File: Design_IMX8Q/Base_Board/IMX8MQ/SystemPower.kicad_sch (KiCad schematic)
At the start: 71 parts, among them Q1 AO3401A, U4 MP8759GD-Z, U5 MP2263GD-Z

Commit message: Add QSPI and more color
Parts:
- removed C1, C10, C2, C3, C4, C5, C6, C7, C8, C9: 4.7uF, Capacitor_SMD:C_0402_1005Metric, symbol Device:C_Small
- removed C11, C12, C13: 22uF, Capacitor_SMD:C_0805_2012Metric, symbol Device:C_Small
- removed C14: 22uF, Capacitor_SMD:C_0402_1005Metric, symbol Device:C_Small
- removed C15, C16: 10uF, Capacitor_SMD:C_0805_2012Metric, symbol Device:C_Small
- removed C17, C64, C65, C66: 0.1uF, Capacitor_SMD:C_0402_1005Metric, symbol Device:C_Small
- removed C18, C63: 1uF, Capacitor_SMD:C_0402_1005Metric, symbol Device:C_Small
- removed C31, C32, C33, C34, C35, C36, C37, C38, C39, C40, C41, C42, C43, C44, C45, C46, C47, C55, C56, C57, C58: 22uF, Capacitor_SMD:C_0603_1608Metric, symbol Device:C_Small
- removed C48, C49, C50, C51, C52, C53: 4.7uF, Capacitor_SMD:C_0603_1608Metric, symbol Device:C_Small
- removed C54: 1uF, Capacitor_SMD:C_0603_1608Metric, symbol Device:C_Small
- removed C59: 220uF, symbol Device:C_Polarized_Small
- removed C60, C61, C62: 0.47uF, Capacitor_SMD:C_0402_1005Metric, symbol Device:C_Small
- removed L1: 1.5uH, Inductor_SMD:L_7.3x7.3_H4.5, symbol Device:L_Small
- removed L2: 4.7uH, Inductor_SMD:L_Taiyo-Yuden_NR-40xx, symbol Device:L_Small
- removed L3, L4, L5, L6, L7: 1uH, Inductor_SMD:L_Taiyo-Yuden_NR-30xx_HandSoldering, symbol Device:L_Small
- removed Q1: AO3401A, Package_TO_SOT_SMD:SOT-23, symbol Transistor_FET:AO3401A
- removed R3: 1.5M, Resistor_SMD:R_0402_1005Metric, symbol Device:R_Small
- removed R4: 44.2K, Resistor_SMD:R_0402_1005Metric, symbol Device:R_Small
- removed R5: 9.53k, Resistor_SMD:R_0402_1005Metric, symbol Device:R_Small
- removed R6, R7: 100k, Resistor_SMD:R_0402_1005Metric, symbol Device:R_Small
- removed R8: 10K, Resistor_SMD:R_0402_1005Metric, symbol Device:R_Small
- removed U3: ~, Package_DFN_QFN:QFN-56-1EP_8x8mm_P0.5mm_EP4.3x4.3mm, symbol _W_MX8M:MC34PF4210
- removed U4: MP8759GD-Z, _W_SBC:MP8759GD-Z, symbol MP8759GD-Z:MP8759GD-Z
- removed U5: MP2263GD-Z, _W_SBC:MP2263, symbol MP2263:MP2263GD-Z
- added U1: MIMX8MQ6CVAHZAB, IMX8MQ_footprints:MIMX8MQ6CVAHZAB, symbol _MIMX8MQ6CVAHZAB:MIMX8MQ6CVAHZAB
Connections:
- net GND: now also U1.A2 (VSS), U1.A24 (VSS), U1.AA16 (VSS), U1.AA21 (VSS), U1.AA5 (VSS), U1.AB11 (VSS), U1.AB18 (VSS), U1.AB2 (VSS), U1.AB24 (VSS), U1.AB9 (VSS), U1.AC19 (VSS), U1.AC22 (VSS), U1.AC4 (VSS), U1.AD1 (VSS), U1.AD11 (VSS), U1.AD13 (VSS), U1.AD16 (VSS), U1.AD25 (VSS), U1.AD7 (VSS), U1.AD9 (VSS), U1.AE2 (VSS), U1.AE21 (VSS), U1.AE24 (VSS), U1.AE5 (VSS), U1.B1 (VSS), U1.B25 (VSS), U1.C10 (VSS), U1.C13 (VSS), U1.C15 (VSS), U1.C24 (VSS), U1.C8 (VSS), U1.D10 (VSS), U1.D13 (VSS), U1.D15 (VSS), U1.D23 (VSS), U1.E10 (VSS), U1.E13 (VSS), U1.E14 (VSS), U1.E16 (VSS), U1.E19 (VSS), U1.E20 (VSS), U1.E21 (VSS), U1.E22 (VSS), U1.E23 (VSS), U1.E4 (VSS), U1.F10 (VSS), U1.F13 (VSS), U1.F14 (VSS), U1.F16 (VSS), U1.F20 (VSS), U1.G10 (VSS), U1.G13 (VSS), U1.G17 (VSS), U1.G18 (VSS), U1.G24 (VSS), U1.G9 (VSS), U1.H10 (VSS), U1.H11 (VSS), U1.H12 (VSS), U1.H13 (VSS), U1.H17 (VSS), U1.H18 (VSS), U1.H8 (VSS), U1.H9 (VSS), U1.J11 (VSS), U1.J12 (VSS), U1.J13 (VSS), U1.J14 (VSS), U1.J17 (VSS), U1.J18 (VSS), U1.J19 (VSS), U1.J3 (VSS), U1.J8 (VSS), U1.K11 (VSS), U1.K13 (VSSA_FPLL_ARM), U1.K17 (VSS), U1.K18 (VSS), U1.K23 (VSS), U1.K8 (VSS), U1.L11 (VSS), U1.L14 (VSS), U1.L17 (VSS), U1.L8 (VSS), U1.M11 (VSS), U1.M14 (VSS), U1.M17 (VSS), U1.M8 (VSS), U1.N12 (VSSA_SPLL_VIDEO2), U1.N14 (VSS), U1.N15 (VSS), U1.N16 (VSS), U1.N17 (VSS), U1.N18 (VSS), U1.N3 (VSS), U1.P11 (VSS), U1.P14 (VSS), U1.P17 (VSS), U1.P18 (VSS), U1.P23 (VSS), U1.P6 (VSS), U1.P8 (VSS), U1.R7 (VSS), U1.T10 (VSS), U1.T11 (VSS), U1.T12 (VSS), U1.T13 (VSS), U1.T14 (VSSA_SPLL_DRAM), U1.T3 (VSS), U1.T4 (VSS), U1.T9 (VSS), U1.U15 (VSS), U1.U16 (VSSA_FPLL), U1.U18 (VSS), U1.U8 (VSS), U1.U9 (VSS), U1.V16 (VSS), U1.V17 (VSSA_SPLL), U1.V23 (VSSA_XTAL_25M), U1.V4 (VSS), U1.V8 (VSS), U1.W1 (VSS), U1.W10 (VSS), U1.W11 (VSS), U1.W12 (VSS), U1.W13 (VSS), U1.W14 (VSS), U1.W15 (VSS), U1.W16 (VSS), U1.W22 (VSSA_XTAL_27M), U1.W25 (VSS), U1.W7 (VSS), U1.W8 (VSS), U1.W9 (VSS), U1.Y11 (VSS), U1.Y13 (VSS), U1.Y15 (VSS), U1.Y17 (VSS), U1.Y19 (VSS), U1.Y2 (VSS), U1.Y21 (VSS), U1.Y22 (VSS), U1.Y23 (VSS), U1.Y24 (VSS), U1.Y3 (VSS), U1.Y4 (VSS), U1.Y5 (VSS), U1.Y7 (VSS), U1.Y9 (VSS)
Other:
- note removed: "10v"
- note removed: "25v"
- note removed: "35v"
- note removed: "50v"

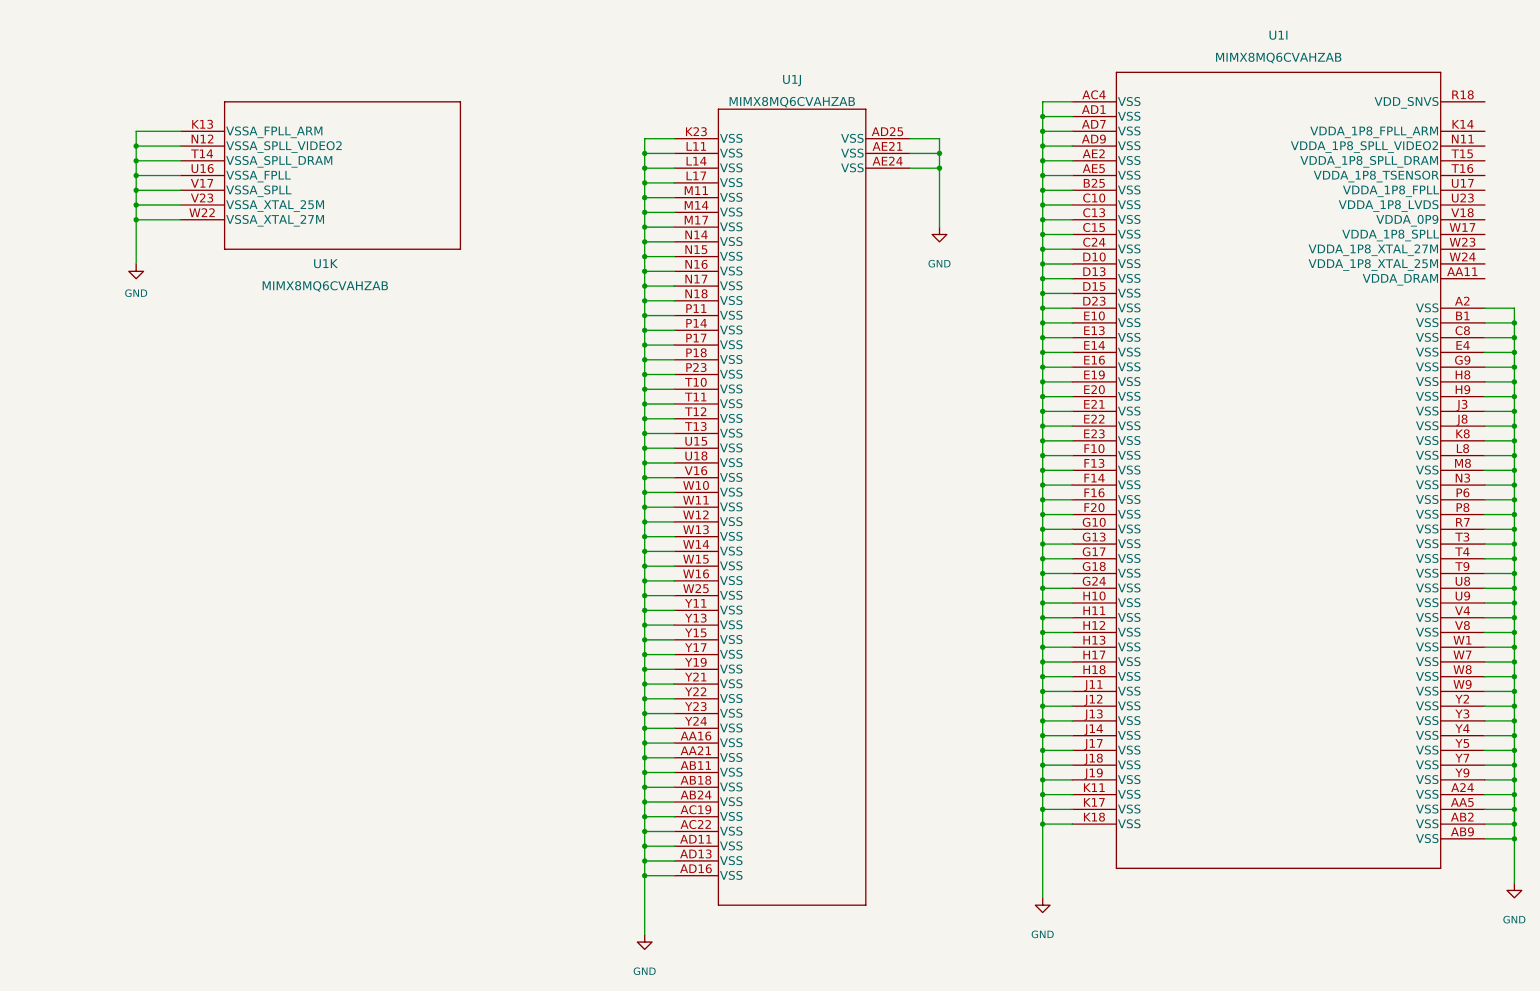
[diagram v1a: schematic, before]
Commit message: it was inserted power control system
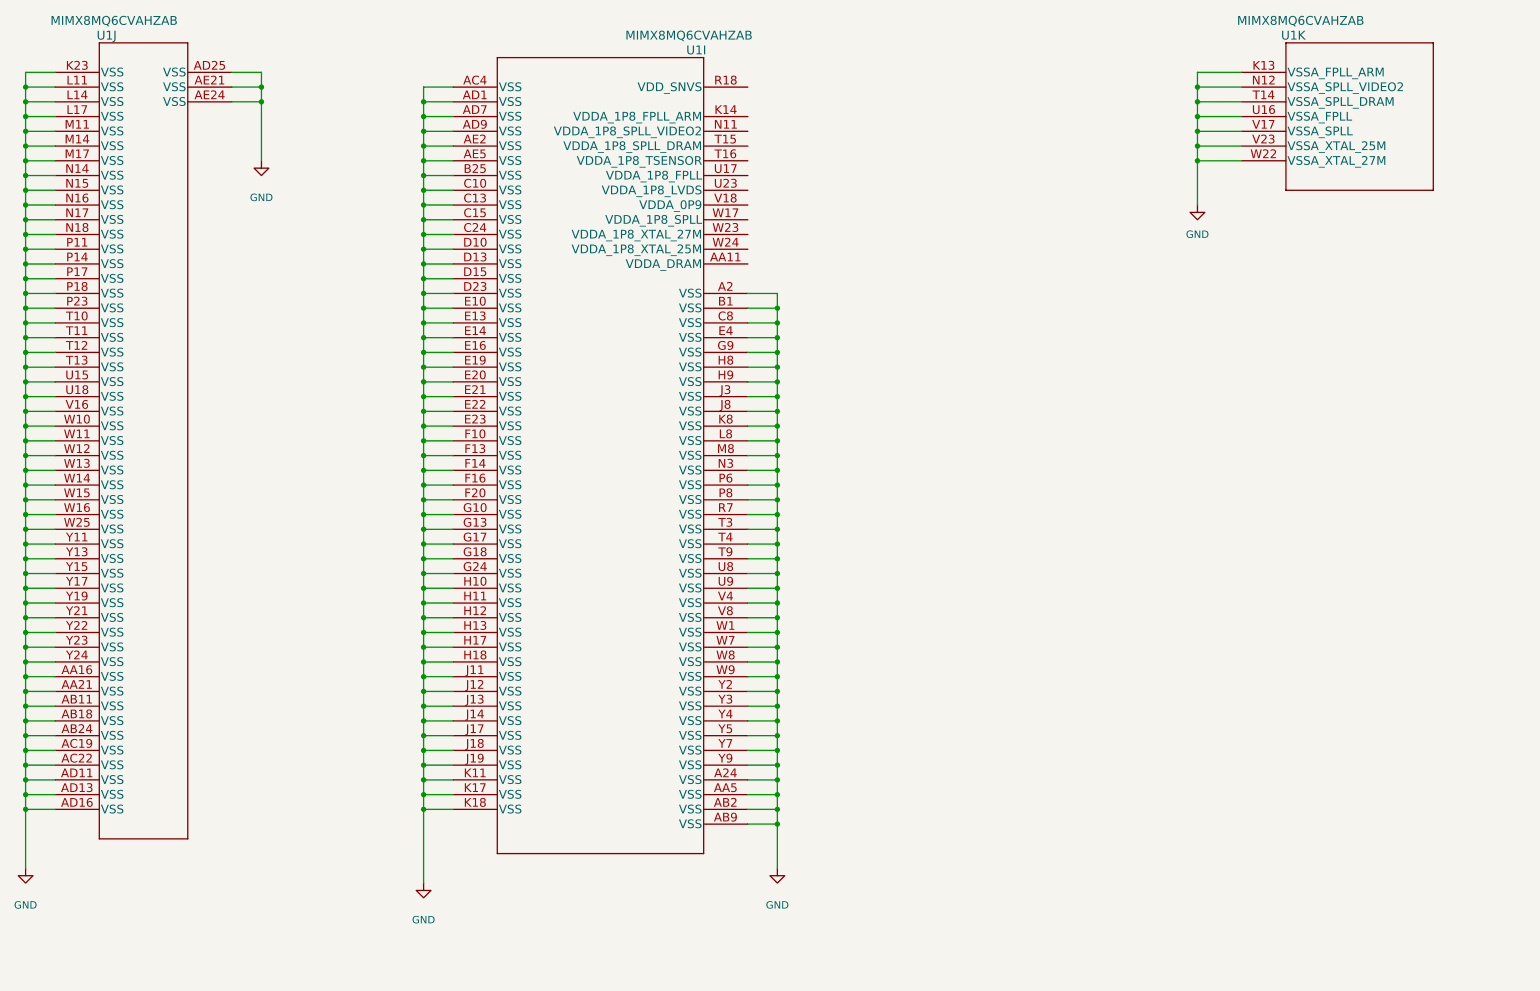
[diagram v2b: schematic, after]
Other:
- moved on the sheet: U1I, U1J, U1K
